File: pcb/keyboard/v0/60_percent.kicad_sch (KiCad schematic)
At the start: 126 parts

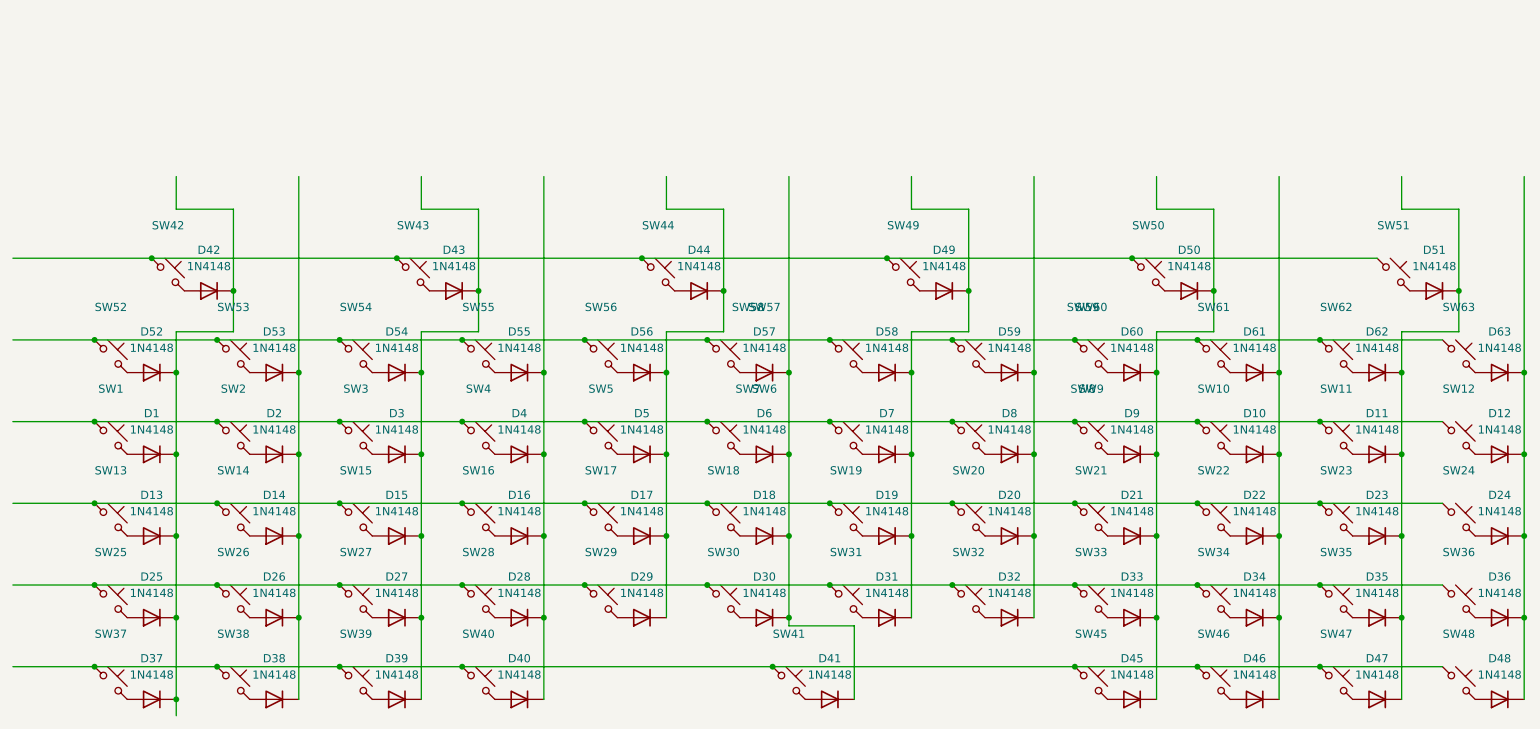
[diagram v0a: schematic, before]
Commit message: Finish keyboard v0 design
This is an early version of the keyboard whose only purpose is to be a
prototype while I'm working on the firmware for it. Its not to scale, it
doesn't have an MCU, and its made entirely out of through-hole
components.
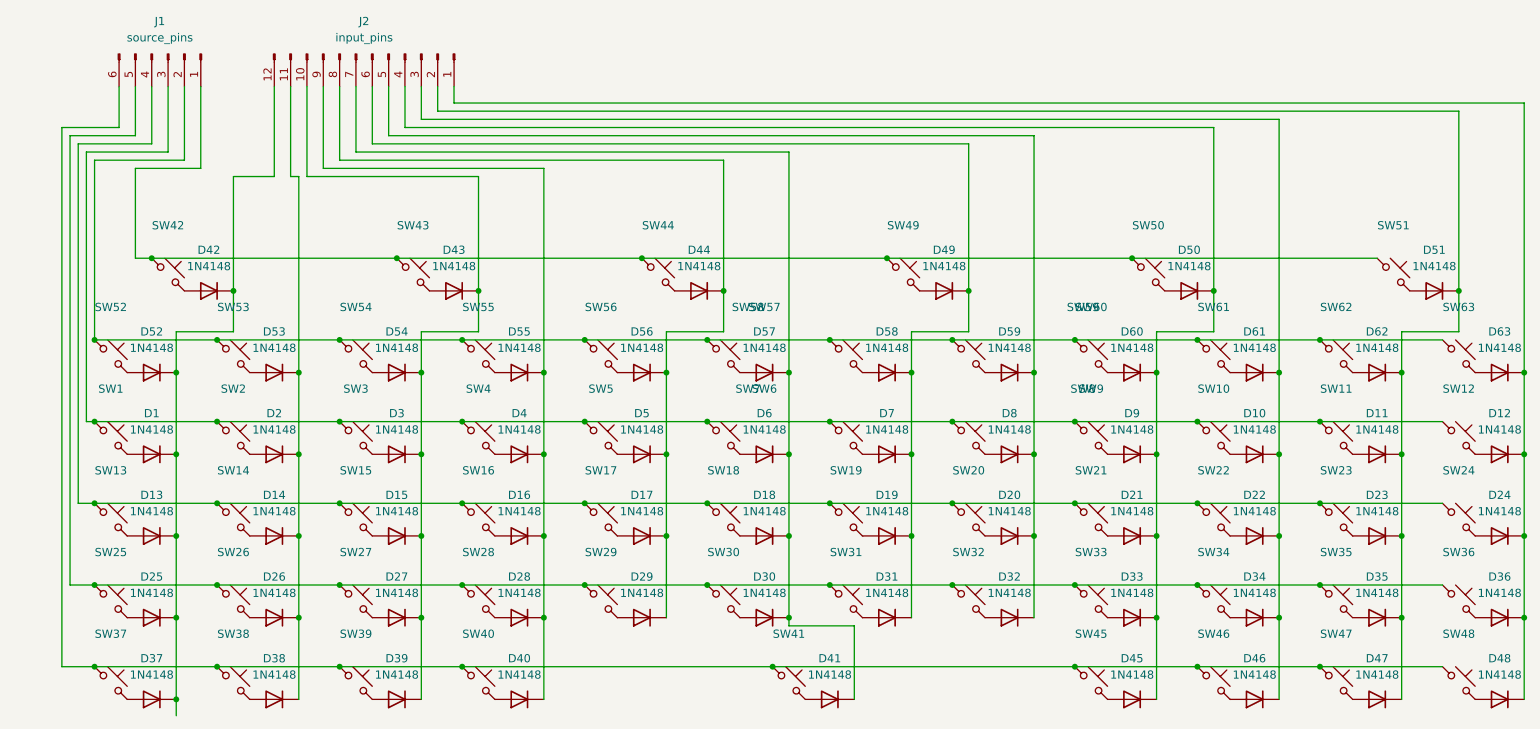
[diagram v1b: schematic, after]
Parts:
- added J1: source_pins, Connector_PinHeader_2.54mm:PinHeader_1x06_P2.54mm_Vertical, symbol Connector:Conn_01x06_Pin
- added J2: input_pins, Connector_PinHeader_2.54mm:PinHeader_1x12_P2.54mm_Vertical, symbol Connector:Conn_01x12_Pin
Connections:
- net at D21.1 (K), D33.1 (K), D45.1 (K)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: now also J2.4 (Pin_4)
- net at D15.1 (K), D27.1 (K), D3.1 (K)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: now also J2.10 (Pin_10)
- net at SW13.1, SW14.1, SW15.1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: now also J1.4 (Pin_4)
- net at SW52.1, SW53.1, SW54.1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: now also J1.2 (Pin_2)
- net at SW42.1, SW43.1, SW44.1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: now also J1.1 (Pin_1)
- net at SW25.1, SW26.1, SW27.1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: now also J1.5 (Pin_5)
- net at SW37.1, SW38.1, SW39.1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: now also J1.6 (Pin_6)
- net at D14.1 (K), D2.1 (K), D26.1 (K)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: now also J2.11 (Pin_11)
- net at D1.1 (K), D13.1 (K), D25.1 (K)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: now also J2.12 (Pin_12)
- net at SW1.1, SW10.1, SW11.1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: now also J1.3 (Pin_3)
- net at D10.1 (K), D22.1 (K), D34.1 (K)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: now also J2.3 (Pin_3)
- net at D17.1 (K), D29.1 (K), D44.1 (K)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: now also J2.8 (Pin_8)
- net at D12.1 (K), D24.1 (K), D36.1 (K)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: now also J2.1 (Pin_1)
- net at D19.1 (K), D31.1 (K), D49.1 (K)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: now also J2.6 (Pin_6)
- net at D11.1 (K), D23.1 (K), D35.1 (K)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: now also J2.2 (Pin_2)
- net at D20.1 (K), D32.1 (K), D59.1 (K)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: now also J2.5 (Pin_5)
- net at D18.1 (K), D30.1 (K), D41.1 (K)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: now also J2.7 (Pin_7)
- net at D16.1 (K), D28.1 (K), D4.1 (K)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: now also J2.9 (Pin_9)
